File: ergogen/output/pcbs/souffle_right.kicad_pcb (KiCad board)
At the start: 2 copper layers, 130 x 99.4 mm, 60 parts

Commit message: feat: choc version
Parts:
- S1, S10, S11, S12, S13, S14, S15, S16, S17, S18, S19, S2, S20, S21, S22, S23, S24, S25, S26, S27, S28, S3, S4, S5, S6, S7, S8, S9: footprint CPG1316S01D02_mikeholscher -> ceoloide:switch_choc_v1_v2; moved to B.Cu
- moved D4 15.1 mm to (357.2, 46.0), turned to 90 degrees
- moved S4 15.1 mm to (365.0, 47.5), turned to -180 degrees
- moved D3 15.0 mm to (357.2, 63.5), turned to 90 degrees
- moved S3 15.0 mm to (365.0, 65.0), turned to -180 degrees
- moved D2 15.0 mm to (357.2, 81.0), turned to 90 degrees
- moved S2 15.0 mm to (365.0, 82.5), turned to -180 degrees
- moved D1 15.0 mm to (357.2, 98.5), turned to 90 degrees
- moved S1 15.0 mm to (365.0, 100.0), turned to -180 degrees
- moved D8 13.6 mm to (338.8, 46.0), turned to 90 degrees
- moved S8 13.6 mm to (346.5, 47.5), turned to -180 degrees
- moved D7 13.5 mm to (338.8, 63.5), turned to 90 degrees
- moved S7 13.5 mm to (346.5, 65.0), turned to -180 degrees
- moved D6 13.5 mm to (338.8, 81.0), turned to 90 degrees
- moved S6 13.5 mm to (346.5, 82.5), turned to -180 degrees
- moved D5 13.5 mm to (338.8, 98.5), turned to 90 degrees
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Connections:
- S1 pad 1: mirror_outer_bottom -> C0
- S1 pad 2: C0 -> mirror_outer_bottom
- S10 pad 1: mirror_ring_home -> C2
- S10 pad 2: C2 -> mirror_ring_home
- S11 pad 1: mirror_ring_top -> C2
- S11 pad 2: C2 -> mirror_ring_top
- S12 pad 1: mirror_ring_number -> C2
- S12 pad 2: C2 -> mirror_ring_number
- S13 pad 1: mirror_middle_bottom -> C3
- S13 pad 2: C3 -> mirror_middle_bottom
- S14 pad 1: mirror_middle_home -> C3
- S14 pad 2: C3 -> mirror_middle_home
- S15 pad 1: mirror_middle_top -> C3
- S15 pad 2: C3 -> mirror_middle_top
- S16 pad 1: mirror_middle_number -> C3
- S16 pad 2: C3 -> mirror_middle_number
- S17 pad 1: mirror_index_bottom -> C4
- S17 pad 2: C4 -> mirror_index_bottom
- S18 pad 1: mirror_index_home -> C4
- S18 pad 2: C4 -> mirror_index_home
- S19 pad 1: mirror_index_top -> C4
- S19 pad 2: C4 -> mirror_index_top
- S2 pad 1: mirror_outer_home -> C0
- S2 pad 2: C0 -> mirror_outer_home
- S20 pad 1: mirror_index_number -> C4
- S20 pad 2: C4 -> mirror_index_number
- S21 pad 1: mirror_inner_bottom -> C5
- S21 pad 2: C5 -> mirror_inner_bottom
- S22 pad 1: mirror_inner_home -> C5
- S22 pad 2: C5 -> mirror_inner_home
- S23 pad 1: mirror_inner_top -> C5
- S23 pad 2: C5 -> mirror_inner_top
- S24 pad 1: mirror_inner_number -> C5
- S24 pad 2: C5 -> mirror_inner_number
- S25 pad 1: mirror_inward_home -> C2
- S25 pad 2: C2 -> mirror_inward_home
- S26 pad 1: mirror_outward_home -> C3
- S26 pad 2: C3 -> mirror_outward_home
- S27 pad 1: mirror_small_thumbkey_home -> C4
- S27 pad 2: C4 -> mirror_small_thumbkey_home
- S28 pad 1: mirror_thumbkey_home -> C5
- S28 pad 2: C5 -> mirror_thumbkey_home
- S3 pad 1: mirror_outer_top -> C0
- S3 pad 2: C0 -> mirror_outer_top
- S4 pad 1: mirror_outer_number -> C0
- S4 pad 2: C0 -> mirror_outer_number
- S5 pad 1: mirror_pinky_bottom -> C1
- S5 pad 2: C1 -> mirror_pinky_bottom
- S6 pad 1: mirror_pinky_home -> C1
- S6 pad 2: C1 -> mirror_pinky_home
- S7 pad 1: mirror_pinky_top -> C1
- S7 pad 2: C1 -> mirror_pinky_top
- S8 pad 1: mirror_pinky_number -> C1
- S8 pad 2: C1 -> mirror_pinky_number
- S9 pad 1: mirror_ring_bottom -> C2
- S9 pad 2: C2 -> mirror_ring_bottom
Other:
- board size 130 x 99.4 mm -> 140.1 x 101.8 mm

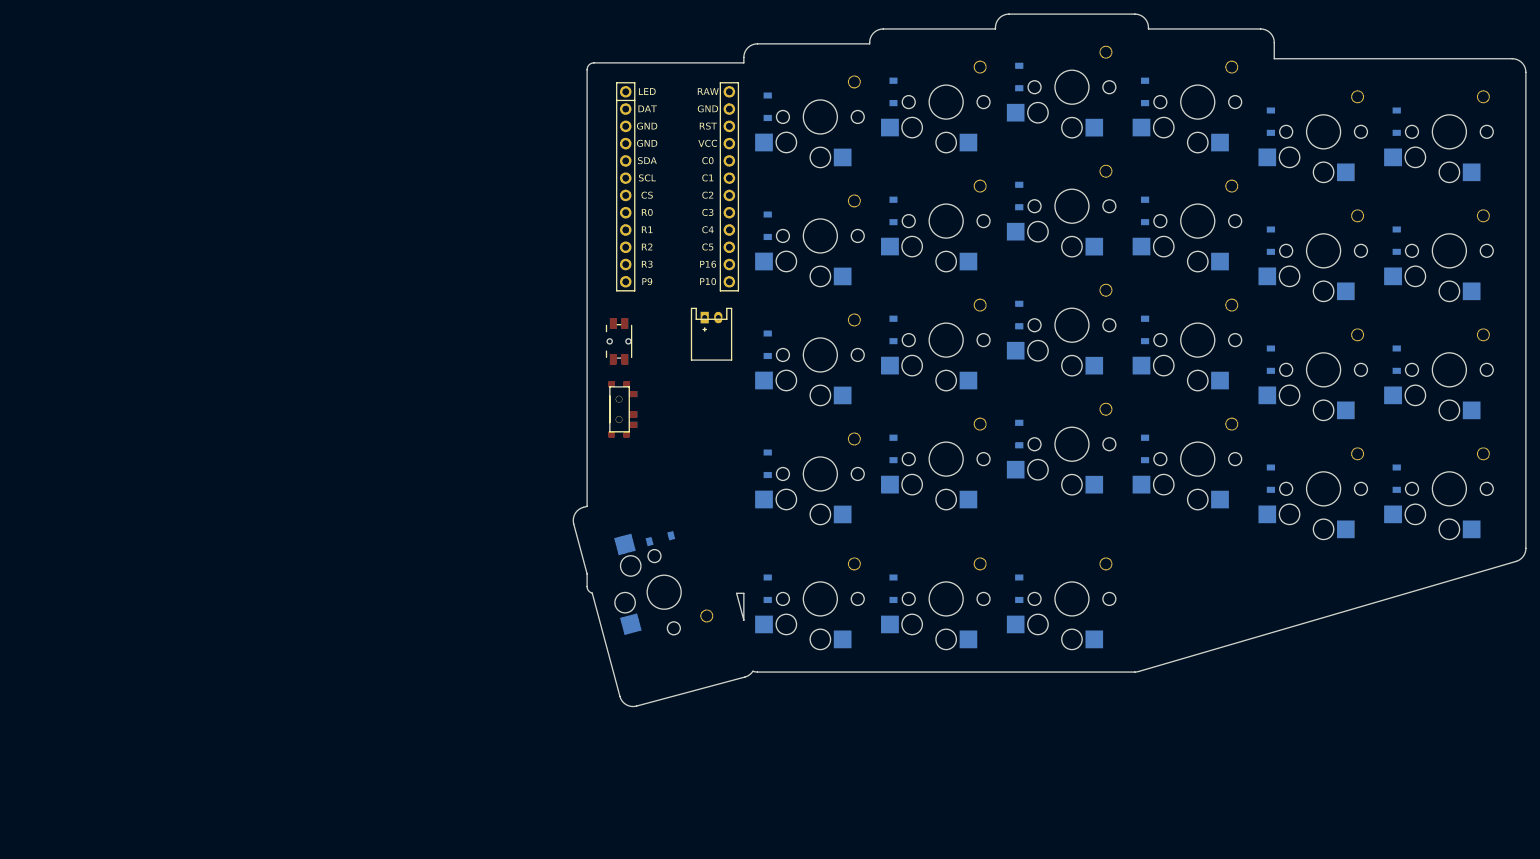
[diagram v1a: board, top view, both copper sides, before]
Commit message: feat: moved mcu to the back and shortened its supporting tab
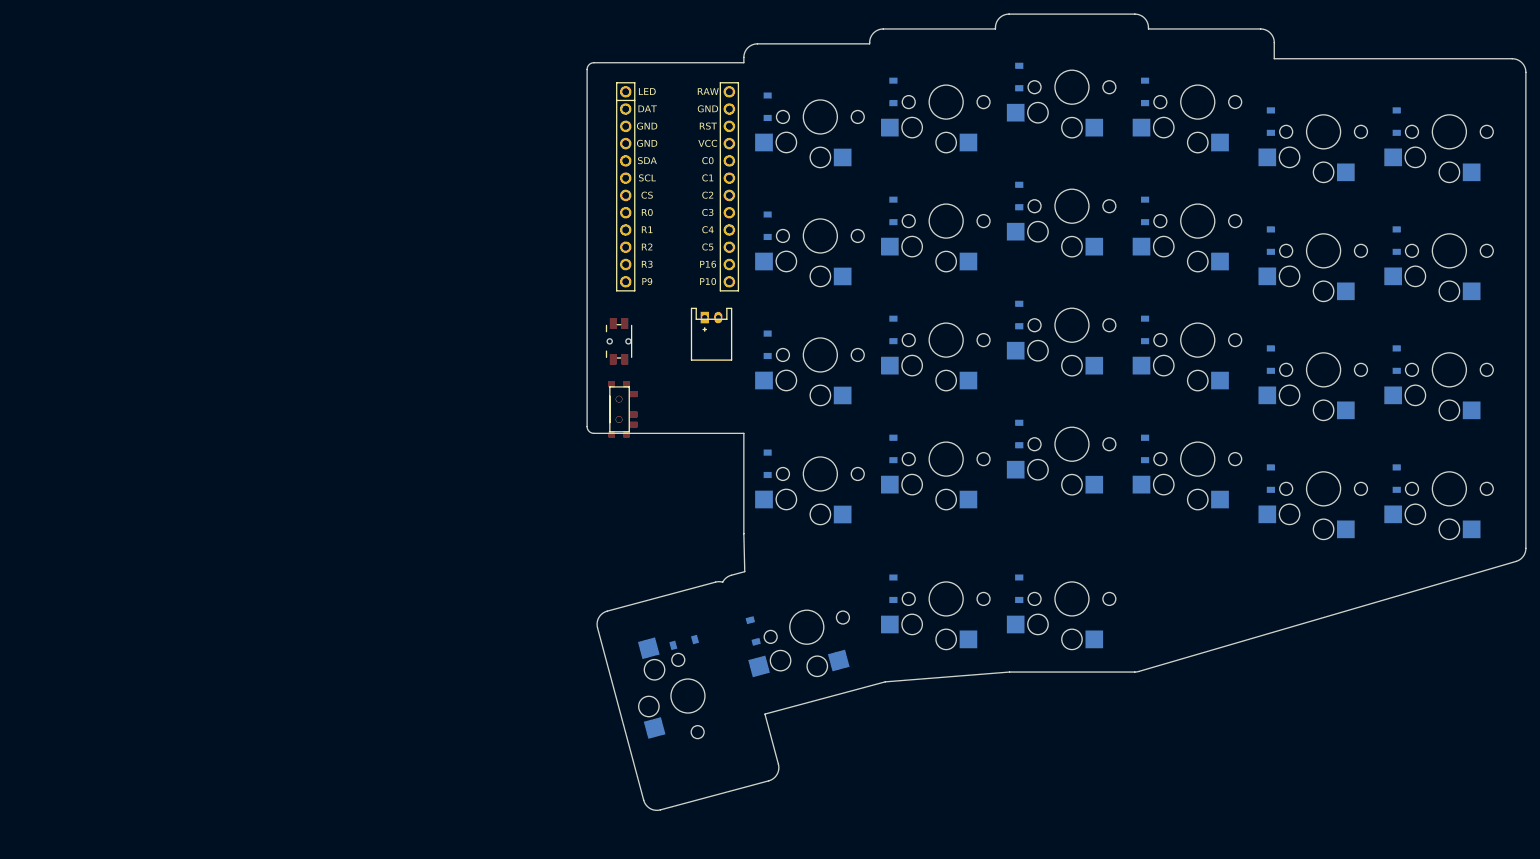
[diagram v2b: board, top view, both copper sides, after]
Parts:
- moved D28 15.7 mm to (252.5, 122.6)
- moved S28 15.7 mm to (253.0, 130.5)
- moved D27 6.56 mm to (262.6, 120.9), turned to 105 degrees
- moved S27 4.61 mm to (270.5, 120.3), turned to -165 degrees
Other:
- board size 140.1 x 101.8 mm -> 138.1 x 117.1 mm

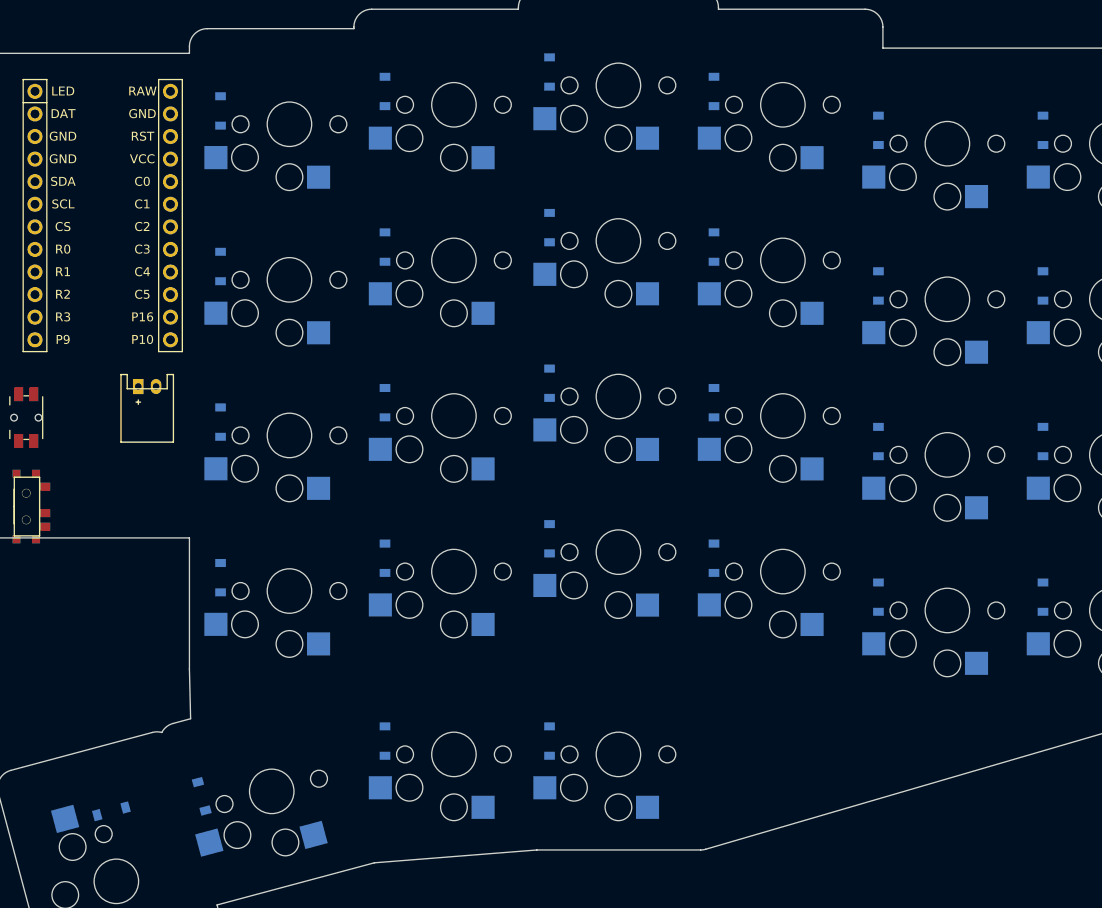
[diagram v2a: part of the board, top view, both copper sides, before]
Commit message: feat: left hand mcu and buttons on the back
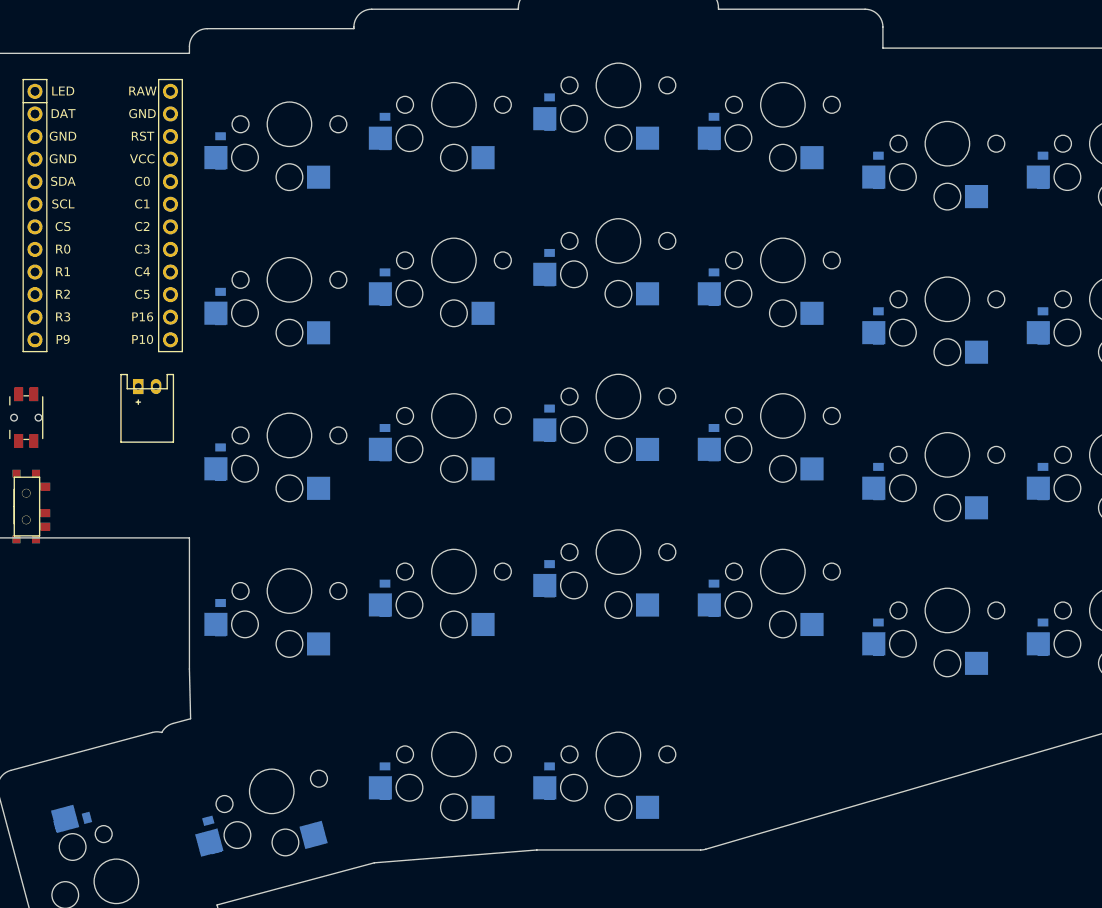
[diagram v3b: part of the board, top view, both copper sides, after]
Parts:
- moved D1 4.50 mm to (357.2, 103.0)
- moved D10 4.50 mm to (320.2, 81.1)
- moved D11 4.50 mm to (320.2, 63.6)
- moved D12 4.50 mm to (320.2, 46.1)
- moved D13 4.50 mm to (301.8, 96.4)
- moved D14 4.50 mm to (301.8, 78.9)
- moved D15 4.50 mm to (301.8, 61.4)
- moved D16 4.50 mm to (301.8, 43.9)
- moved D17 4.50 mm to (283.2, 98.6)
- moved D18 4.50 mm to (283.2, 81.1)
- moved D19 4.50 mm to (283.2, 63.6)
- moved D2 4.50 mm to (357.2, 85.5)
- moved D20 4.50 mm to (283.2, 46.1)
- moved D21 4.50 mm to (264.8, 100.8)
- moved D22 4.50 mm to (264.8, 83.3)
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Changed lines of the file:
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@@
     (footprint "ceoloide:diode_tht_sod123"
         (layer "B.Cu")
-        (at 357.25 98.5 90)
+        (at 357.25 103 90)
         (property "Reference" "D1"
             (at 0 0 90)
@@
     (footprint "ceoloide:diode_tht_sod123"
         (layer "B.Cu")
-        (at 357.25 81 90)
+        (at 357.25 85.5 90)
         (property "Reference" "D2"
             (at 0 0 90)
@@
     (footprint "ceoloide:diode_tht_sod123"
         (layer "B.Cu")
-        (at 357.25 63.5 90)
+        (at 357.25 68 90)
         (property "Reference" "D3"
             (at 0 0 90)
@@
     (footprint "ceoloide:diode_tht_sod123"
         (layer "B.Cu")
-        (at 357.25 46 90)
+        (at 357.25 50.5 90)
         (property "Reference" "D4"
             (at 0 0 90)
@@
     (footprint "ceoloide:diode_tht_sod123"
         (layer "B.Cu")
-        (at 338.75 98.5 90)
+        (at 338.75 103 90)
         (property "Reference" "D5"
             (at 0 0 90)
@@
     (footprint "ceoloide:diode_tht_sod123"
         (layer "B.Cu")
-        (at 338.75 81 90)
+        (at 338.75 85.5 90)
         (property "Reference" "D6"
             (at 0 0 90)
@@
     (footprint "ceoloide:diode_tht_sod123"
         (layer "B.Cu")
-        (at 338.75 63.5 90)
+        (at 338.75 68 90)
         (property "Reference" "D7"
             (at 0 0 90)
@@
     (footprint "ceoloide:diode_tht_sod123"
         (layer "B.Cu")
-        (at 338.75 46 90)
+        (at 338.75 50.5 90)
         (property "Reference" "D8"
             (at 0 0 90)
@@
     (footprint "ceoloide:diode_tht_sod123"
         (layer "B.Cu")
-        (at 320.25 94.125 90)
+        (at 320.25 98.625 90)
         (property "Reference" "D9"
             (at 0 0 90)
@@
     (footprint "ceoloide:diode_tht_sod123"
         (layer "B.Cu")
-        (at 320.25 76.625 90)
+        (at 320.25 81.125 90)
         (property "Reference" "D10"
             (at 0 0 90)
@@
     (footprint "ceoloide:diode_tht_sod123"
         (layer "B.Cu")
-        (at 320.25 59.125 90)
+        (at 320.25 63.625 90)
         (property "Reference" "D11"
             (at 0 0 90)
@@
     (footprint "ceoloide:diode_tht_sod123"
         (layer "B.Cu")
-        (at 320.25 41.625 90)
+        (at 320.25 46.125 90)
         (property "Reference" "D12"
             (at 0 0 90)
@@
     (footprint "ceoloide:diode_tht_sod123"
         (layer "B.Cu")
-        (at 301.75 91.9375 90)
+        (at 301.75 96.4375 90)
         (property "Reference" "D13"
             (at 0 0 90)
@@
     (footprint "ceoloide:diode_tht_sod123"
         (layer "B.Cu")
-        (at 301.75 74.4375 90)
+        (at 301.75 78.9375 90)
         (property "Reference" "D14"
             (at 0 0 90)
@@
     (footprint "ceoloide:diode_tht_sod123"
         (layer "B.Cu")
-        (at 301.75 56.9375 90)
+        (at 301.75 61.4375 90)
         (property "Reference" "D15"
             (at 0 0 90)
@@
     (footprint "ceoloide:diode_tht_sod123"
         (layer "B.Cu")
-        (at 301.75 39.4375 90)
+        (at 301.75 43.9375 90)
         (property "Reference" "D16"
             (at 0 0 90)
@@
     (footprint "ceoloide:diode_tht_sod123"
         (layer "B.Cu")
-        (at 283.25 94.125 90)
+        (at 283.25 98.625 90)
         (property "Reference" "D17"
             (at 0 0 90)
@@
     (footprint "ceoloide:diode_tht_sod123"
         (layer "B.Cu")
-        (at 283.25 76.625 90)
+        (at 283.25 81.125 90)
         (property "Reference" "D18"
             (at 0 0 90)
@@
     (footprint "ceoloide:diode_tht_sod123"
         (layer "B.Cu")
-        (at 283.25 59.125 90)
+        (at 283.25 63.625 90)
         (property "Reference" "D19"
             (at 0 0 90)
@@
     (footprint "ceoloide:diode_tht_sod123"
         (layer "B.Cu")
-        (at 283.25 41.625 90)
+        (at 283.25 46.125 90)
         (property "Reference" "D20"
             (at 0 0 90)
@@
     (footprint "ceoloide:diode_tht_sod123"
         (layer "B.Cu")
-        (at 264.75 96.3125 90)
+        (at 264.75 100.8125 90)
         (property "Reference" "D21"
             (at 0 0 90)
@@
     (footprint "ceoloide:diode_tht_sod123"
         (layer "B.Cu")
-        (at 264.75 78.8125 90)
+        (at 264.75 83.3125 90)
         (property "Reference" "D22"
             (at 0 0 90)
@@
     (footprint "ceoloide:diode_tht_sod123"
         (layer "B.Cu")
-        (at 264.75 61.3125 90)
+        (at 264.75 65.8125 90)
         (property "Reference" "D23"
             (at 0 0 90)
@@
     (footprint "ceoloide:diode_tht_sod123"
         (layer "B.Cu")
-        (at 264.75 43.8125 90)
+        (at 264.75 48.3125 90)
         (property "Reference" "D24"
             (at 0 0 90)
@@
     (footprint "ceoloide:diode_tht_sod123"
         (layer "B.Cu")
-        (at 301.75 114.6875 90)
+        (at 301.75 119.1875 90)
         (property "Reference" "D25"
             (at 0 0 90)
@@
     (footprint "ceoloide:diode_tht_sod123"
         (layer "B.Cu")
-        (at 283.25 114.6875 90)
+        (at 283.25 119.1875 90)
         (property "Reference" "D26"
             (at 0 0 90)
@@
     (footprint "ceoloide:diode_tht_sod123"
         (layer "B.Cu")
-        (at 262.63393549999995 120.9016564 105)
+        (at 263.79862119999996 125.2483226 105)
         (property "Reference" "D27"
             (at 0 0 105)
@@
     (footprint "ceoloide:diode_tht_sod123"
         (layer "B.Cu")
-        (at 252.4743766 122.58862580000002 15)
+        (at 248.1277104 123.75331150000001 15)
         (property "Reference" "D28"
             (at 0 0 15)
